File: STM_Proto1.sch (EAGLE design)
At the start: 81 parts, among them IC1 LM358D, Q1 8M, Q2 32748

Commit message: Libraries for Simholder and HM-10
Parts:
- removed JP2: (no value), pinhead:PINHD-1X4
- removed SV1: (no value), con-lstb:MA03-1
- removed U$1: SIMHOLDER3, SparkFun-Connectors:SIMHOLDER3
- added E1: HM-10-BOARD, JNHuaMao:HM-10-BOARD
- added JP1: (no value), pinhead:PINHD-1X4
- added LED4: (no value), led:LEDCHIPLED_1206
- added R26, R27: 470, resistor:R-EU_R0805
- added R28: reset, resistor:R-EU_R1206
- added U$3: SIMHOLDER3, SparkFun-Connectors:SIMHOLDER3
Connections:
- removed net +3V3: SV1.3
- removed net A0.0+: IC1A.OUT, R25.1, SV1.1
- removed net ADC_RES: STM32L152CBT6.PB0
- new net ADC_TERM: IC1A.OUT, R25.1, STM32L152CBT6.PB0
- new net I2C_SCL: JP1.3, STM32L152CBT6.PB6
- new net I2C_SDA: JP1.4, STM32L152CBT6.PB7
- new net N$26: E1.LED, R26.2
- new net N$27: LED4.A, R26.1
- new net N$37: E1.KEY, R27.2, R28.2
- net 3.3V: now also E1.+3.3V, JP1.1, R27.1
- net CTS: no longer JP2.1
- net DCD: no longer JP2.4
- net DTR: no longer JP2.3
- net GND: now also E1.GND, JP1.2, LED4.C, R28.1, U$3.GND; no longer SV1.2, U$1.GND
- net N$10: now also U$3.VCC; no longer U$1.VCC
- net N$14: now also U$3.RST; no longer U$1.RST
- net N$16: now also U$3.CLK; no longer U$1.CLK
- net N$18: now also U$3.I/O; no longer U$1.I/O
- net RTS: no longer JP2.2
- net USART2_RX: now also E1.UART_TX
- net USART2_TX: now also E1.UART_RX
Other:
- note added: "BLE 4.0"
- note added: "STM32"
- note added: "Supply"
- note added: "Termo"
- moved on the sheet: AUDIO, C1, C10, C11, C12, C13, C14, C15, C16, C17, C18, C19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

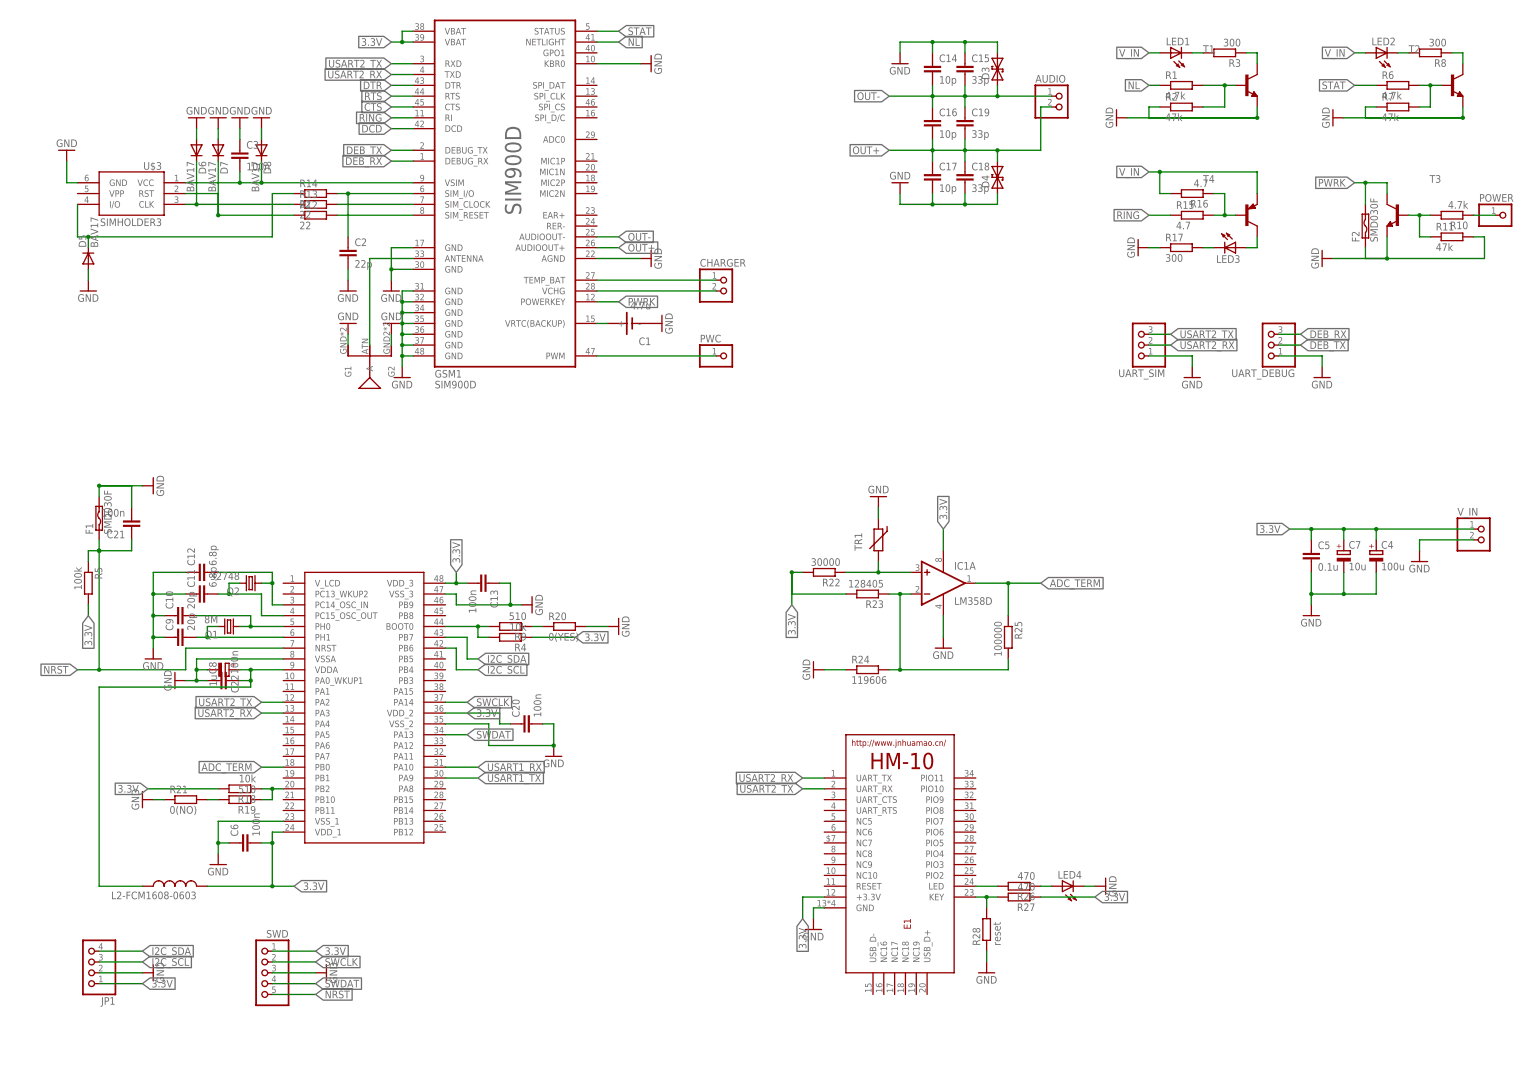
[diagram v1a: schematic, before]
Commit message: Add Charger
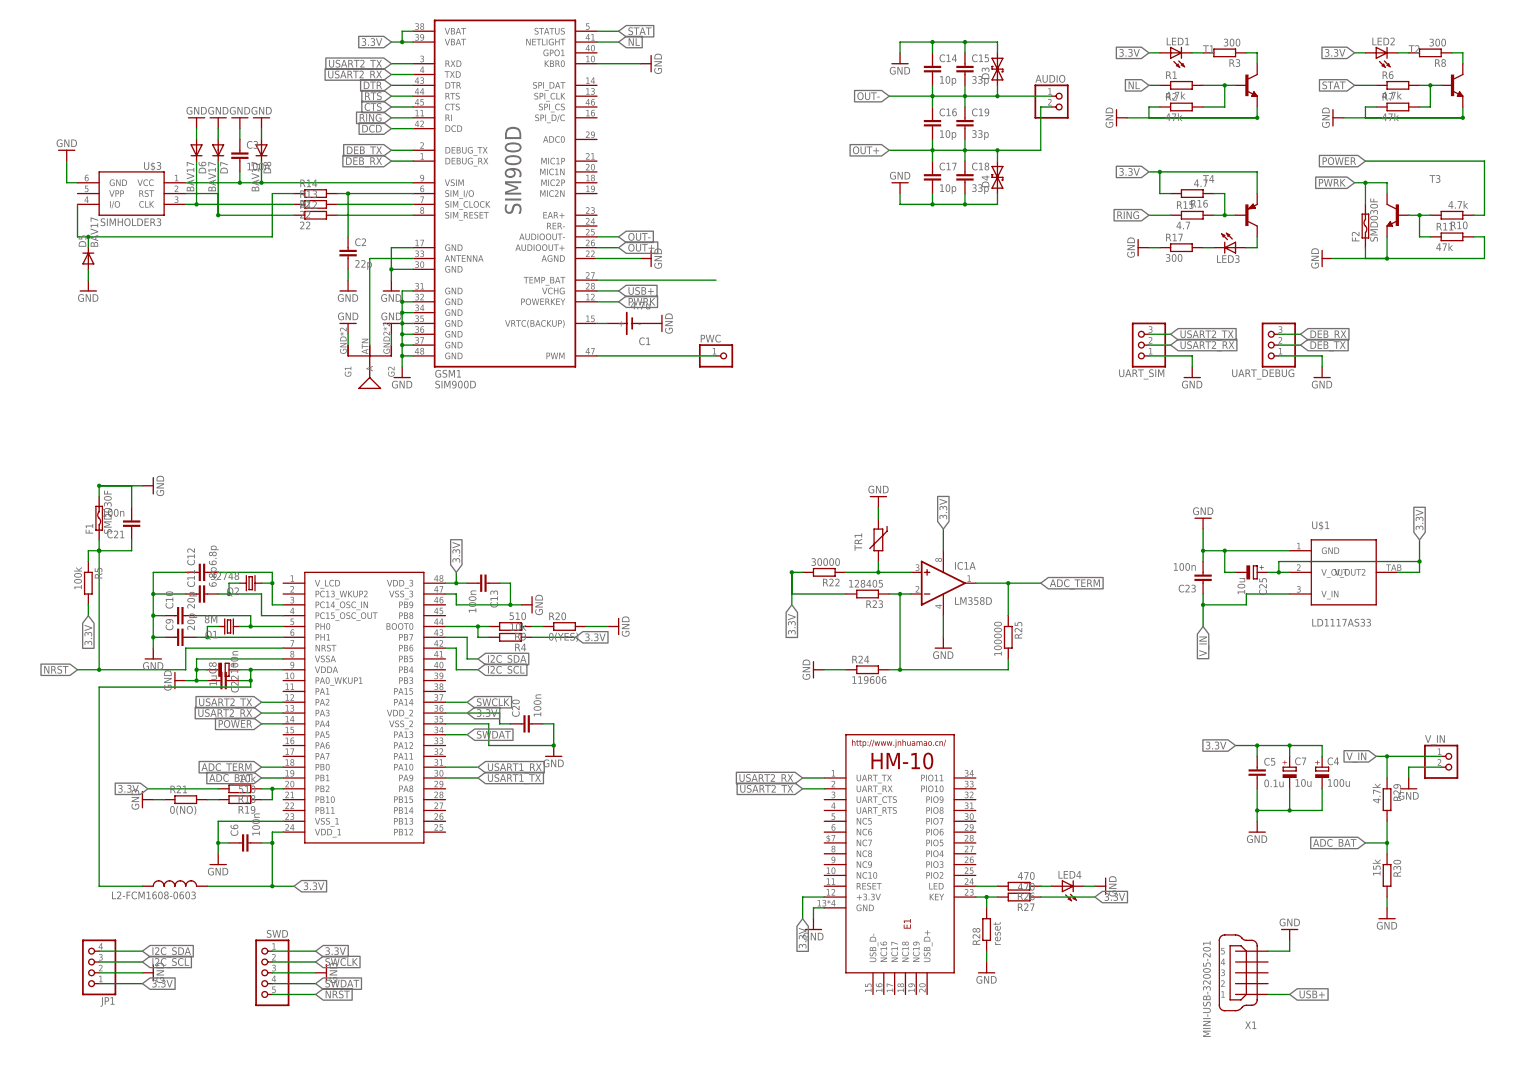
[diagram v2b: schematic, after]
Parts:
- removed CHARGER: (no value), pinhead:PINHD-1X2
- removed POWER: (no value), pinhead:PINHD-1X1
- added C23: 100n, resistor:C-EUC0805
- added C25: 10u, resistor:CPOL-EU153CLV-0405
- added R29: 4.7k, resistor:R-EU_R0805
- added R30: 15k, resistor:R-EU_R0805
- added U$1: LD1117AS33, LD1117AS33:LD1117AS33
- added X1: MINI-USB-32005-201, con-cypressindustries:MINI-USB-32005-201
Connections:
- removed net N$21: CHARGER.2, GSM1.VCHG
- removed net N$6: POWER.1, R10.1
- new net ADC_BAT: R29.2, R30.1, STM32L152CBT6.PB1
- new net POWER: R10.1, STM32L152CBT6.PA4
- new net USB+: GSM1.VCHG, X1.1
- net 3.3V: now also C25.+, LED1.A, LED2.A, R16.2, T4.E, U$1.V_OUT, U$1.V_OUT2; no longer V_IN.1
- net GND: now also C23.2, C25.-, R30.2, U$1.GND, X1.5
- net N$20: no longer CHARGER.1
- net V_IN: now also C23.1, R29.1, U$1.V_IN, V_IN.1; no longer LED1.A, LED2.A, R16.2, T4.E
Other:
- moved on the sheet: C4, C5, C7, V_IN

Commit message: Last version with SIM900D
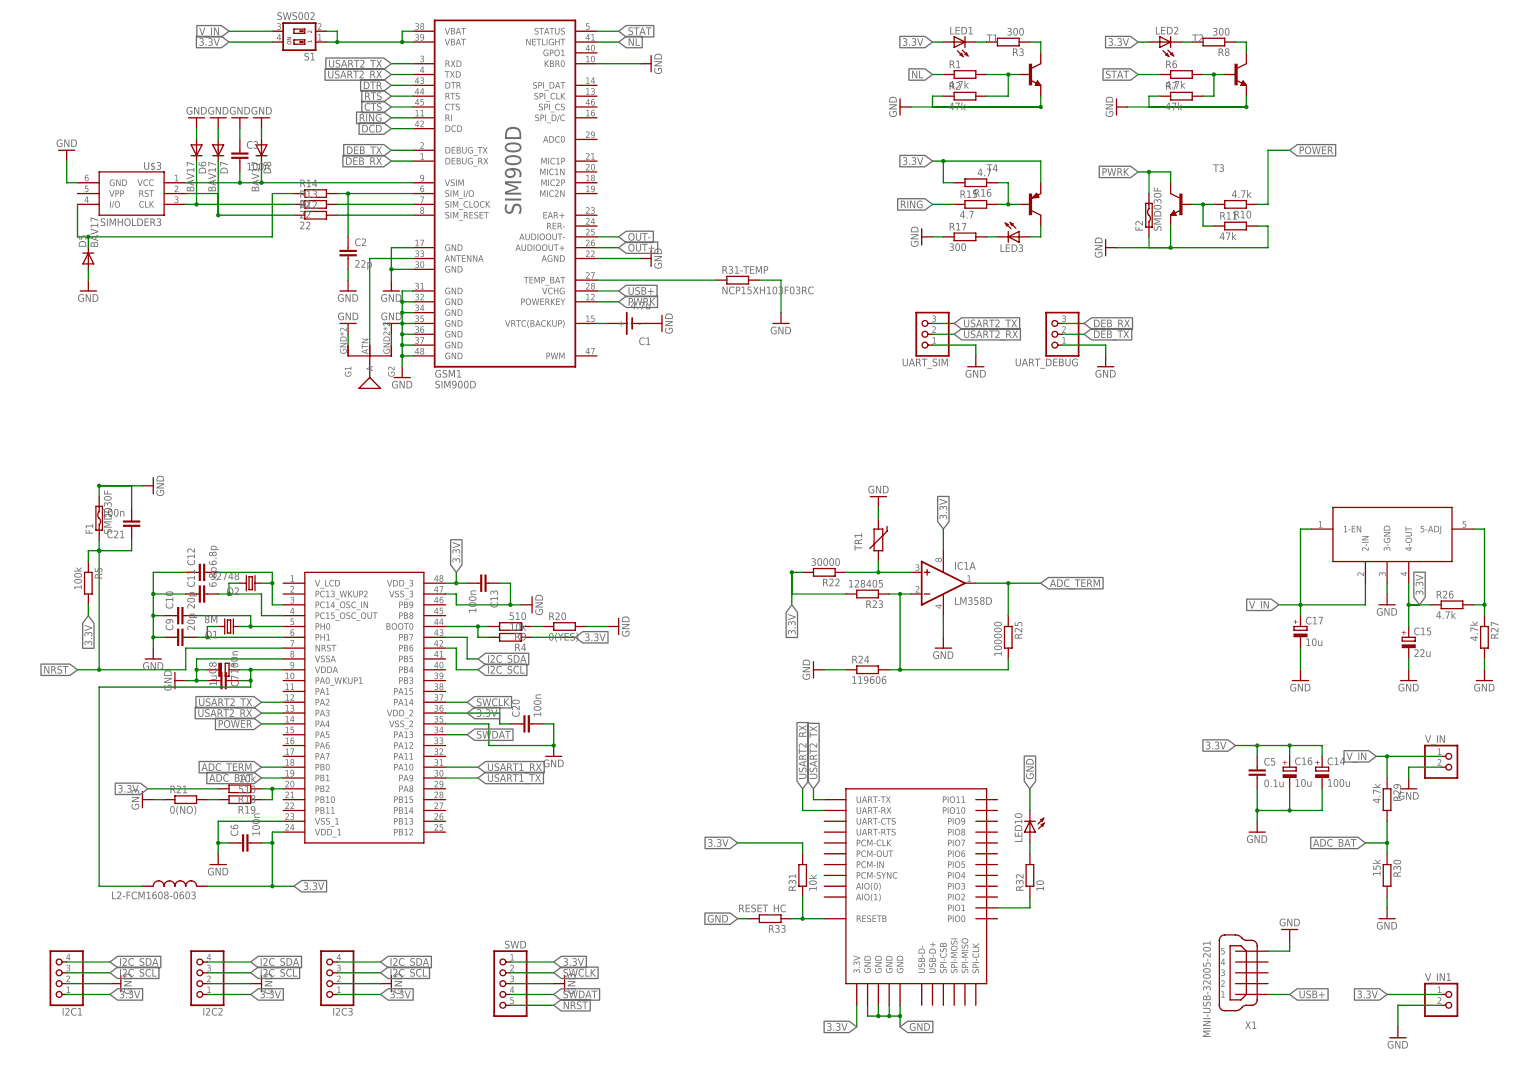
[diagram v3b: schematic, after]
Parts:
- removed AUDIO: (no value), pinhead:PINHD-1X2
- removed C18, C19: 33p, resistor:C-EUC0805
- removed C22: 1u, resistor:CPOL-EUA/3216-18W
- removed C23: 100n, resistor:C-EUC0805
- removed C25: 10u, resistor:CPOL-EU153CLV-0405
- removed C4: 100u, resistor:CPOL-EU153CLV-0605
- removed D3, D4: (no value), diode:DIODE_SCHOTTKY2-F126-12
- removed E1: HM-10-BOARD, JNHuaMao:HM-10-BOARD
- removed JP1: (no value), pinhead:PINHD-1X4
- removed LED4: (no value), led:LEDCHIPLED_1206
- removed PWC: (no value), pinhead:PINHD-1X1
- removed R28: reset, resistor:R-EU_R1206
- removed U$1: LD1117AS33, LD1117AS33:LD1117AS33
- added I2C1, I2C2, I2C3: (no value), pinhead:PINHD-1X4
- added LED10: (no value), led:LEDCHIPLED_1206
- added R31: 10k, resistor:R-EU_M0805
- added R31-TEMP: NCP15XH103F03RC, resistor:R-EU_M0805
- added R32: 10, resistor:R-EU_M0805
- added R33: RESET_HC, resistor:R-EU_M0805
- added S1: SWS002, smd-special:SWS002
- added U$4: (no value), hc-05 eagle lib:BTM400_6B
- added U$5: MIC29302WT, MIC29302WT:MIC29302WT
- added V_IN1: (no value), pinhead:PINHD-1X2
- C14: value 10p -> 100u; device resistor:C-EUC0805 -> resistor:CPOL-EU153CLV-0807
- C15: value 33p -> 22u; device resistor:C-EUC0805 -> resistor:CPOL-EU153CLV-0605
- C16, C17: value 10p -> 10u; device resistor:C-EUC0805 -> resistor:CPOL-EU153CLV-0505
- C3: device resistor:C-EUC1206 -> resistor:C-EUC0805
- C7: value 10u -> 1u
- R26, R27: value 470 -> 4.7k
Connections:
- removed net N$26: E1.LED, R26.2
- removed net N$27: LED4.A, R26.1
- removed net N$37: E1.KEY, R27.2, R28.2
- removed net N$7: GSM1.PWM, PWC.1
- new net N$21: R32.1, U$4.PIO1
- new net N$33: LED10.A, R32.2
- new net N$38: R26.2, R27.1, U$5.5-ADJ
- new net N$6: R31.1, R33.1, U$4.RESETB
- new net VBAT@2: GSM1.VBAT@1, GSM1.VBAT@2, S1.1, S1.2
- net 3.3V: now also C14.+, C15.+, C16.+, I2C1.1, I2C2.1, I2C3.1, R26.1, R31.2, S1.4, U$4.3.3V, U$5.4-OUT, V_IN1.1; no longer C25.+, C4.+, C7.+, E1.+3.3V, GSM1.VBAT@1, GSM1.VBAT@2, JP1.1, R27.1, U$1.V_OUT, U$1.V_OUT2
- net GND: now also C14.-, C15.-, C16.-, C17.-, I2C1.2, I2C2.2, I2C3.2, LED10.C, R27.2, R31-TEMP.2, R33.2, U$4.GND@1, U$4.GND@2, U$4.GND@3, U$4.GND@4, U$5.3-GND, V_IN1.2; no longer C14.1, C15.1, C17.2, C18.2, C22.-, C23.2, C25.-, C4.-, D3.2, D4.1, E1.GND, JP1.2, LED4.C, R28.1, U$1.GND
- net I2C_SCL: now also I2C1.3, I2C2.3, I2C3.3; no longer JP1.3
- net I2C_SDA: now also I2C1.4, I2C2.4, I2C3.4; no longer JP1.4
- net N$20: now also R31-TEMP.1
- net N$31: now also C7.+; no longer C22.+
- net OUT+: no longer AUDIO.2, C16.2, C17.1, C18.1, C19.2, D4.2
- net OUT-: no longer AUDIO.1, C14.2, C15.2, C16.1, C19.1, D3.1
- net USART2_RX: now also U$4.UART-RX; no longer E1.UART_TX
- net USART2_TX: now also U$4.UART-TX; no longer E1.UART_RX
- net V_IN: now also C17.+, S1.3, U$5.1-EN, U$5.2-IN; no longer C23.1, U$1.V_IN
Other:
- note removed: "AUDIO_OUT"
- moved on the sheet: C7, F2, LED1, LED2, LED3, R1, R10, R11, R15, R16, R17, R2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
